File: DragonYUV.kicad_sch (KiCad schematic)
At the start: 73 parts, among them IC1 74HCT273, IC11 74LS123N, IC2 MC6847, J1 Video Output, J2 Board Interconnect Male, J3 JTAG, J4 SVid, Q1 MMBT4401, Q2 NPN, Q3 NPN, Q4 NPN, Q5 NPN, Q6 NPN, U1 AD724JR, U3 ATF1504ASL-xAx44, Y1 4.433620MHz

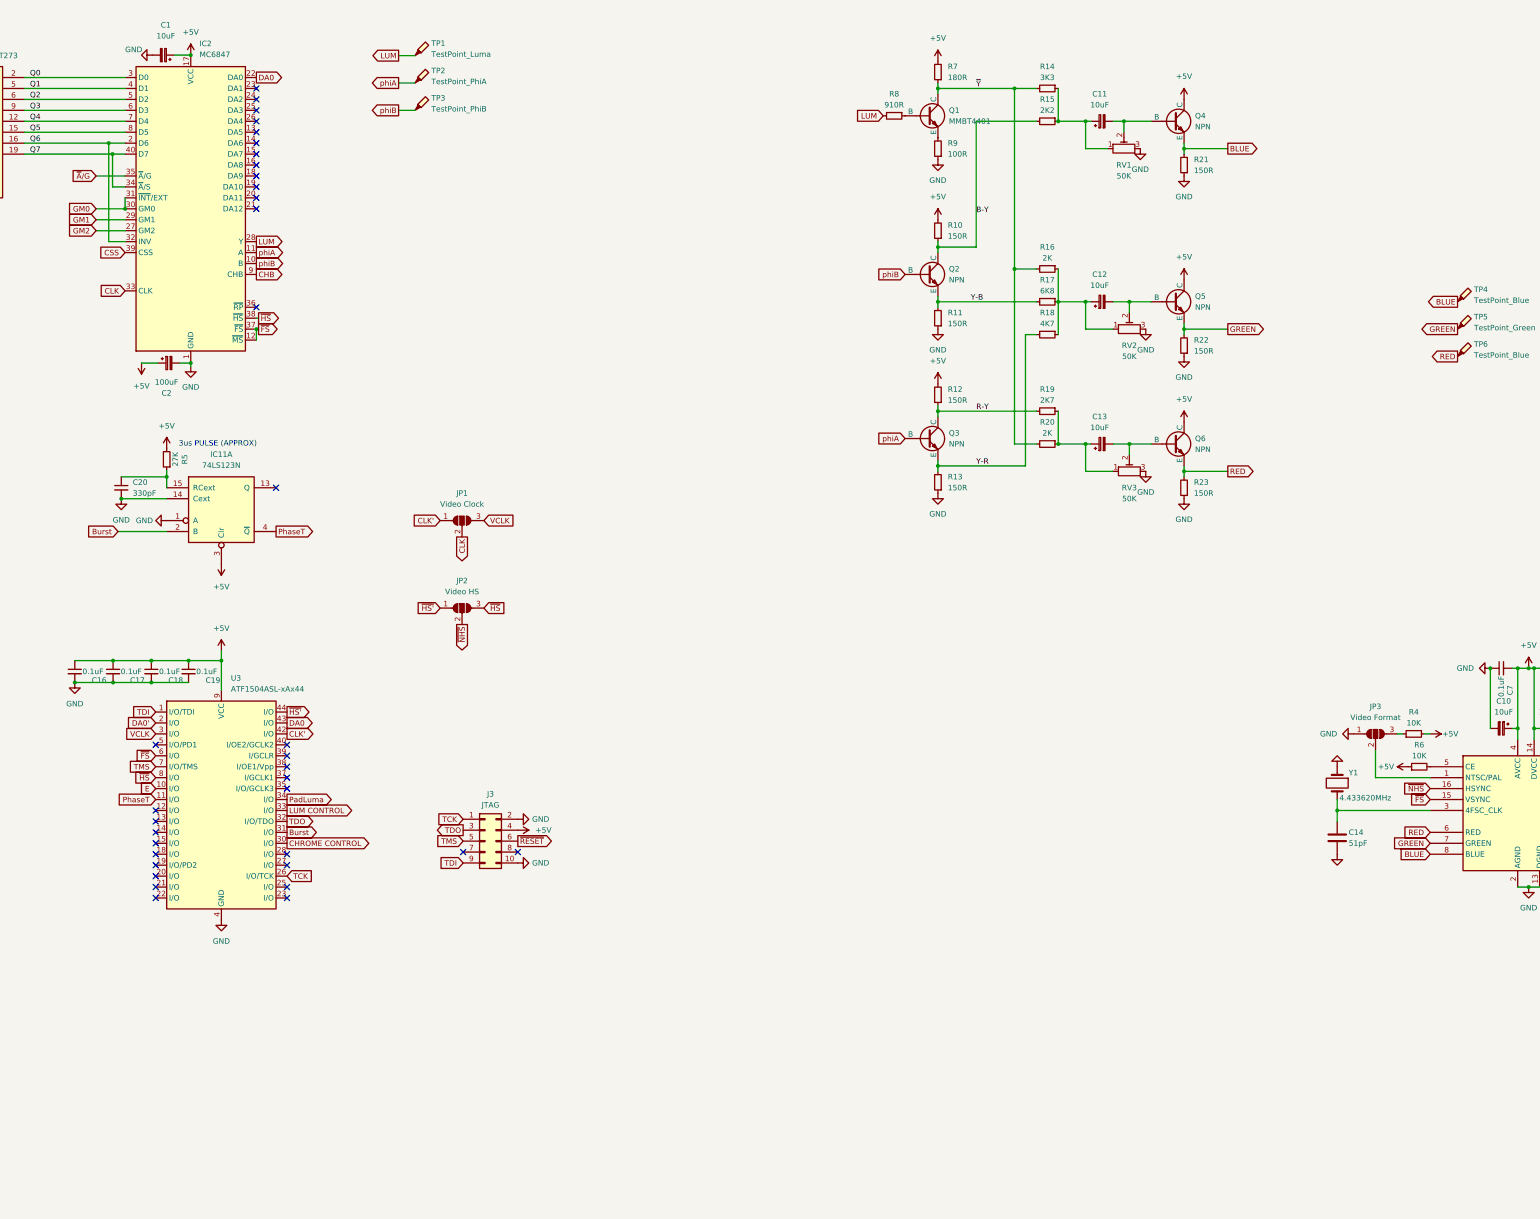
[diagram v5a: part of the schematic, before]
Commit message: rework schematics for demux of video
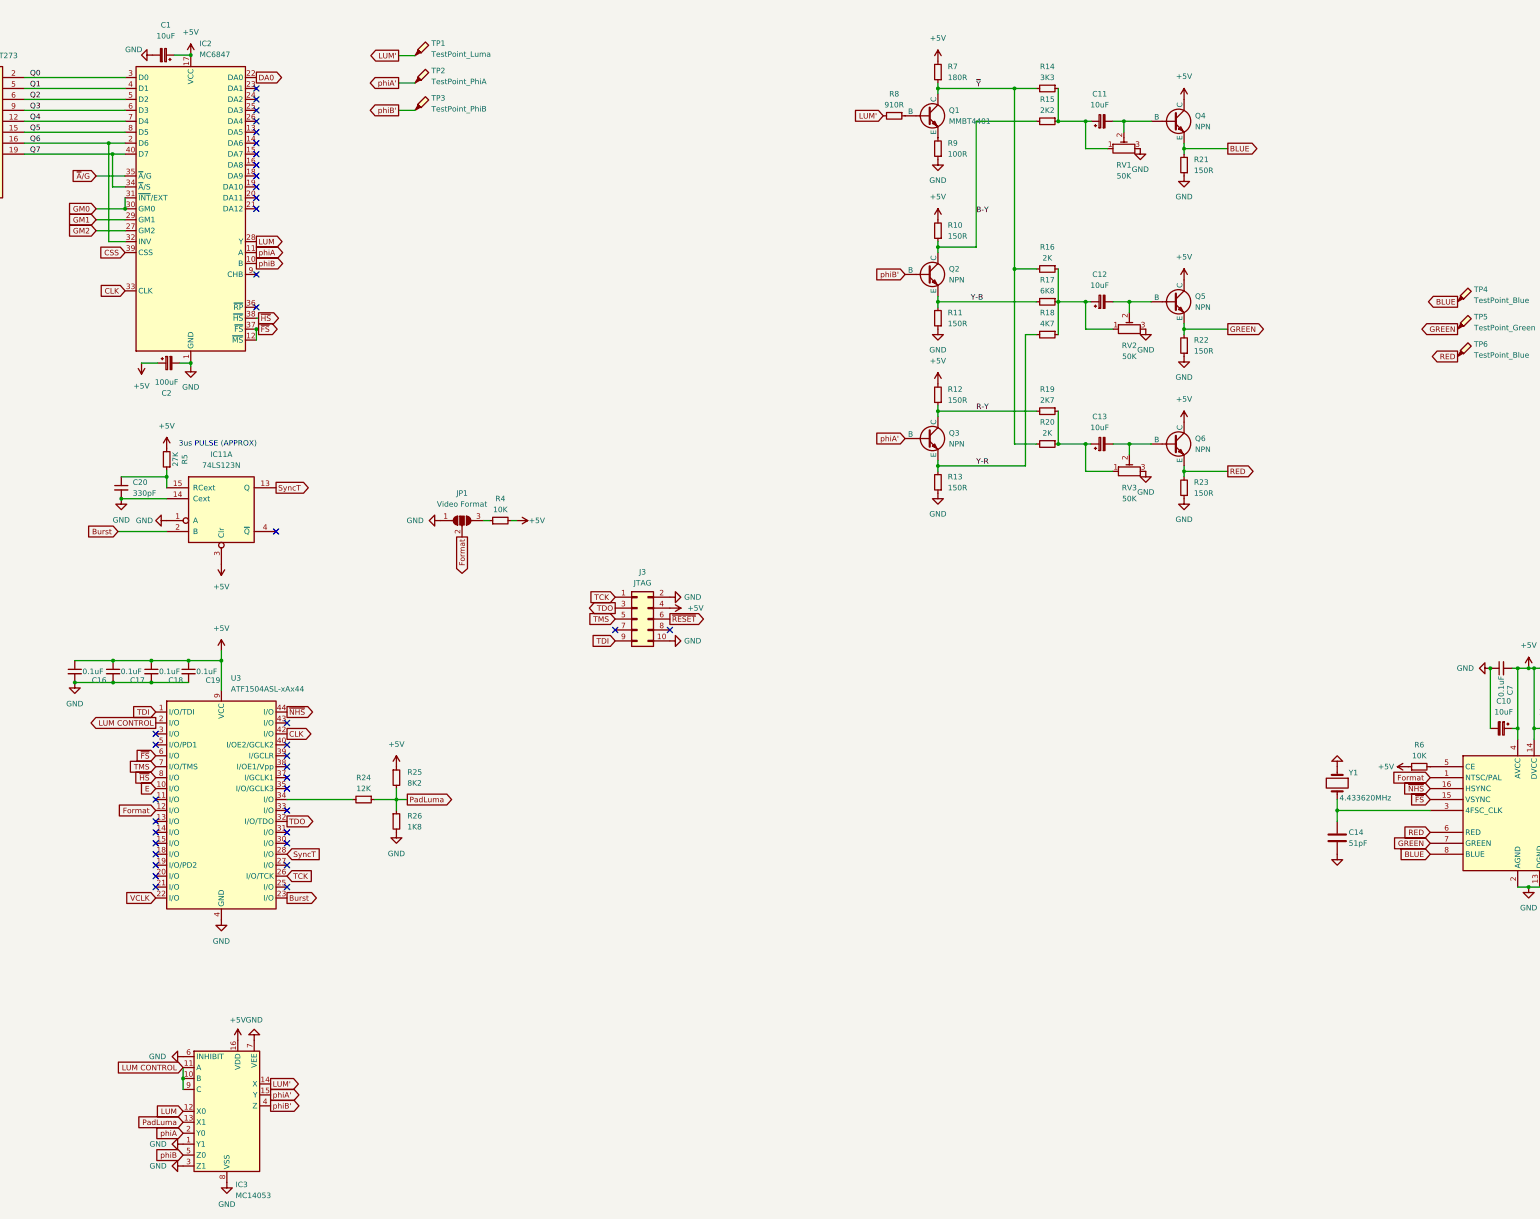
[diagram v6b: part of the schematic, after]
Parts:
- removed JP2: Video HS, Jumper:SolderJumper-3_P1.3mm_Open_Pad1.0x1.5mm_NumberLabels, symbol Jumper:SolderJumper_3_Open
- removed JP3: Video Format, Jumper:SolderJumper-3_P1.3mm_Open_Pad1.0x1.5mm_NumberLabels, symbol Jumper:SolderJumper_3_Open
- added IC3: MC14053, Package_SO:TSSOP-16_4.4x3.6mm_P0.4mm, symbol vdg:MC14053
- added R24: 12K, Resistor_SMD:R_0805_2012Metric_Pad1.20x1.40mm_HandSolder, symbol Device:R_Small
- added R25: 8K2, Resistor_SMD:R_0805_2012Metric_Pad1.20x1.40mm_HandSolder, symbol Device:R_Small
- added R26: 1K8, Resistor_SMD:R_0805_2012Metric_Pad1.20x1.40mm_HandSolder, symbol Device:R_Small
- JP1: value Video Clock -> Video Format
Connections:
- net DA0' is gone; now on net LUM CONTROL: U3.2 (I/O)
- net ~{HS'} is gone; now on net ~{NHS}: U3.44 (I/O)
- net +5V: now also IC3.16 (VDD), R25.1
- net Burst: now also U3.23 (I/O); no longer U3.31 (I/O)
- net CLK: now also U3.42 (I/O); no longer JP1.2 (C)
- net DA0: no longer U3.43 (I/O)
- net GND: now also JP1.1 (A), IC3.1 (Y1), IC3.3 (Z1), IC3.6 (INHIBIT), IC3.7 (VEE), IC3.8 (VSS), R26.2
- net LUM: now also IC3.12 (X0); no longer R8.2, TP1.1
- net LUM CONTROL: now also IC3.10 (B), IC3.11 (A), IC3.9 (C); no longer U3.33 (I/O)
- net PadLuma: now also IC3.13 (X1), R24.1, R25.2, R26.1; no longer U3.34 (I/O)
- net VCLK: now also U3.22 (I/O); no longer JP1.3 (B), U3.3 (I/O)
- net phiA: now also IC3.2 (Y0); no longer Q3.2 (B), TP2.1
- net phiB: now also IC3.5 (Z0); no longer Q2.2 (B), TP3.1
- net SyncT: now reaches IC11.13 (Q)
- net SyncT: now also U3.28 (I/O)
- net Format: now reaches U1.1 (NTSC/PAL)
- net Format: now also JP1.2 (C), U3.12 (I/O)
- net at R4.1: now also JP1.3 (B)
- net CHB: no longer names the net of IC2.9 (CHB)
- net CHROME CONTROL: no longer names the net of U3.30 (I/O)
- removed net CLK': JP1.1 (A), U3.42 (I/O)
- net PhaseT: no longer names the net of IC11.4 (~{Q})
- net PhaseT: no longer U3.11 (I/O)
- new net: R24.2, U3.34 (I/O)
- new net LUM': IC3.14 (X), R8.2, TP1.1
- new net phiA': IC3.15 (Y), Q3.2 (B), TP2.1
- new net phiB': IC3.4 (Z), Q2.2 (B), TP3.1
- no-connect marks 42 -> 45
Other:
- moved on the sheet: J3

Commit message: compose verilog
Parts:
- removed C20: 330pF, Capacitor_SMD:C_0805_2012Metric_Pad1.18x1.45mm_HandSolder, symbol Device:C_Small
- removed IC11: 74LS123N, Package_SO:SOIC-16_3.9x9.9mm_P1.27mm, symbol 74xx:74LS123
- removed R5: 27K, Resistor_SMD:R_0805_2012Metric_Pad1.20x1.40mm_HandSolder, symbol Device:R_Small
- removed TP4, TP6: TestPoint_Blue, TestPoint:TestPoint_Pad_D1.0mm, symbol Connector:TestPoint_Probe
- removed TP5: TestPoint_Green, TestPoint:TestPoint_Pad_D1.0mm, symbol Connector:TestPoint_Probe
- IC1: value 74HCT273 -> 74LS273; footprint Package_SO:TSSOP-20_4.4x6.5mm_P0.65mm -> Package_SO:SOIC-20W_7.5x12.8mm_P1.27mm; DigiKey 296-8409-1-ND -> 296-3682-1-ND
- IC3: footprint Package_SO:TSSOP-16_4.4x3.6mm_P0.4mm -> Package_SO:SOIC-16_3.9x9.9mm_P1.27mm
- J3: footprint Connector_PinHeader_1.27mm:PinHeader_2x05_P1.27mm_Vertical -> Connector_PinHeader_2.54mm:PinHeader_2x05_P2.54mm_Vertical
- R21, R22, R23: footprint Resistor_SMD:R_0805_2012Metric_Pad1.20x1.40mm_HandSolder -> Resistor_SMD:R_0603_1608Metric
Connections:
- net DO4: now also IC1.18 (D7); no longer IC1.13 (D4)
- net DO5: now also IC1.17 (D6); no longer IC1.14 (D5)
- net DO6: now also IC1.14 (D5); no longer IC1.17 (D6)
- net DO7: now also IC1.13 (D4); no longer IC1.18 (D7)
- net GND: now also IC3.13 (X1); no longer IC3.1 (Y1)
- net LUM: now also IC3.2 (Y0); no longer IC3.12 (X0)
- net LUM': now also IC3.15 (Y); no longer IC3.14 (X)
- net PadLuma: now also IC3.1 (Y1); no longer IC3.13 (X1)
- net Q4: now also IC1.19 (Q7); no longer IC1.12 (Q4)
- net Q5: now also IC1.16 (Q6); no longer IC1.15 (Q5)
- net Q6: now also IC1.15 (Q5); no longer IC1.16 (Q6)
- net Q7: now also IC1.12 (Q4); no longer IC1.19 (Q7)
- net phiA: now also IC3.12 (X0); no longer IC3.2 (Y0)
- net phiA': now also IC3.14 (X); no longer IC3.15 (Y)
- net Burst: no longer names the net of U3.23 (I/O)
- net SyncT: no longer names the net of U3.28 (I/O)
- no-connect marks 45 -> 43
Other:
- note removed: "3us PULSE (APPROX)"
- moved on the sheet: C1, C2, IC2
